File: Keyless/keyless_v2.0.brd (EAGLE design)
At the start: 75 x 48.3 mm, 43 parts, among them J1 AVR_SPI_PRG_6NS, U1 USD-SOCKET, X1 USB-SMD-NS, Y1 16MHz

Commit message: reasons
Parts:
- moved C5 1.09 mm to (58.2, 9.78)
- moved C6 1.02 mm to (60.1, 9.78)
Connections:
- removed net 3.3V1: J1.2
- removed net B10: J1.4
- removed net B8: J1.3
- removed net B9: J1.1
- removed net RESET1: J1.5
- net 3.3V: now also J1.2
- net B1: now also J1.3
- net B2: now also J1.4
- net B3: now also J1.1
- net RESET: now also J1.5
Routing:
- net RAW: track 0.00 -> 44.1 mm
- net 5V: track 0.00 -> 41.2 mm
- net N$1: track 0.00 -> 18.5 mm
- net GND: track 0.00 -> 16.6 mm
- net D6: track 0.00 -> 15.8 mm
- net D7: track 0.00 -> 14.2 mm
- net B4: track 0.00 -> 12.7 mm
- net B1: track 0.00 -> 12.1 mm
- net B3: track 0.00 -> 12.1 mm
- net B2: track 0.00 -> 11.4 mm
- net N$12: track 0.00 -> 9.21 mm
- net N$6: track 0.00 -> 8.98 mm
- net N$5: track 0.00 -> 7.75 mm
- net N$4: track 0.00 -> 6.89 mm
- net UVCC: track 0.00 -> 6.44 mm
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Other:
- board text added: "HackManhattan"
- board text added: "KONSGN"

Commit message: more wires!
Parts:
- moved R9 20.1 mm to (45.8, 9.65)
- moved SJ1 19.7 mm to (42.4, 9.65)
- moved X1 19.7 mm to (47.1, 3.94)
- moved R8 19.6 mm to (47.5, 9.65)
- moved JP2 15.2 mm to (27.3, 3.68)
- moved U$3 13.6 mm to (33.8, 11.7)
- moved C13 13.6 mm to (30.1, 13.0)
- moved C19 13.6 mm to (30.1, 10.5)
- moved U$1 4.45 mm to (39.5, 4.83)
- moved R10 3.83 mm to (37.7, 9.40)
- moved J1 3.07 mm to (40.9, 15.9)
- moved C1 0.81 mm to (49.7, 15.2)
- moved C5 0.51 mm to (58.7, 9.78)
- moved R12 0.51 mm to (67.6, 33.8)
- moved R13 0.51 mm to (65.3, 33.8)
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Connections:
- removed net RAW: C19.1, JP2.2, SJ1.1, U$3.3
- net 5V: now also C19.1, JP2.2, SJ1.1, U$3.3
- net B7: now also JP1.7
- net D5: no longer JP1.7
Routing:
- net 5V: track 41.2 -> 128.4 mm
- net B2: track 11.4 -> 56.8 mm, vias 0 -> 2
- net RAW: track 44.1 -> 0.00 mm
- net B0: track 0.00 -> 42.0 mm, vias 0 -> 1
- net B1: track 12.1 -> 51.3 mm, vias 0 -> 1
- net B3: track 12.1 -> 50.9 mm, vias 0 -> 1
- net 3.3V: track 3.85 -> 37.5 mm, vias 0 -> 1
- net RESET: track 5.32 -> 36.7 mm, vias 0 -> 2
- net UVCC: track 6.44 -> 33.5 mm
- net B7: track 0.00 -> 18.8 mm, vias 0 -> 2
- net D+: track 0.00 -> 14.6 mm
- net D-: track 0.00 -> 14.5 mm
- net GND: track 16.6 -> 21.3 mm
- net N$12: track 9.21 -> 10.3 mm
- net AREF: track 2.03 -> 2.72 mm
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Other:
- outline, holes or cut-outs redrawn
- board text added: "BY:"
- board text added: "Konstantin"
- board text added: "Nickolai"

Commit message: more routing!
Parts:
- moved R13 1.82 mm to (64.9, 35.6)
- moved R12 1.82 mm to (67.2, 35.6)
- moved R7 1.82 mm to (69.5, 35.6)
- moved D3 1.82 mm to (64.9, 38.6)
- moved D1 1.82 mm to (69.5, 38.6)
- moved D2 1.82 mm to (67.2, 38.6)
- moved C2 0.50 mm to (71.9, 20.6)
- moved C4 0.50 mm to (71.9, 15.5)
- moved Y1 0.50 mm to (68.8, 18.0)
- moved C1 0.45 mm to (49.7, 15.7)
- moved R10 0.40 mm to (37.3, 9.27)
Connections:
- removed net N$20: U1.CD1
- removed net N$21: U1.CD2
- net F4: now also U1.CD1
- net GND: now also U1.CD2
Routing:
- net B5: track 0.00 -> 105.6 mm
- net 3.3V: track 37.5 -> 130.9 mm, vias 1 -> 6
- net F4: track 0.00 -> 34.0 mm, vias 0 -> 1
- net F0: track 2.16 -> 31.3 mm
- net D4: track 0.00 -> 28.8 mm, vias 0 -> 2
- net F1: track 3.87 -> 17.7 mm
- net GND: track 21.3 -> 12.8 mm, vias 0 -> 21
- net D0: track 0.00 -> 7.12 mm, vias 0 -> 1
- net B7: track 18.8 -> 20.2 mm
- net N$12: track 10.3 -> 10.9 mm
- net RESET: track 36.7 -> 37.3 mm
- net D6: track 16.1 -> 16.7 mm
- net D7: track 14.6 -> 15.2 mm

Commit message: more stuffs
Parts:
- moved JP3 29.5 mm to (91.6, 27.3), turned to 0 degrees
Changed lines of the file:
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@@
 <setting verticaltext="up"/>
 </settings>
-<grid distance="0.1" unitdist="mm" unit="mm" style="lines" multiple="1" display="yes" altdistance="0.025" altunitdist="inch" altunit="inch"/>
+<grid distance="1.25" unitdist="mil" unit="mil" style="lines" multiple="1" display="yes" altdistance="0.025" altunitdist="inch" altunit="inch"/>
 <layers>
 <layer number="1" name="Top" color="4" fill="1" visible="yes" active="yes"/>
@@
 <element name="R13" library="SparkFun" package="0805" value="330" x="64.878" y="35.56" rot="R90"/>
 <element name="D3" library="led" package="CHIP-LED0805" value="Green" x="64.878" y="38.608"/>
-<element name="JP3" library="SparkFun-Connectors" package="1X08" value="" x="73.406" y="4.064" rot="R180"/>
+<element name="JP3" library="SparkFun-Connectors" package="1X08" value="" x="91.60795" y="27.251390625"/>
 </elements>
 <signals>

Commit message: more
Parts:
- moved JP3 61.4 mm to (30.3, 30.0)
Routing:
- net GND: track 12.8 -> 15.1 mm
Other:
- board text added: "5V in"
- board text added: "GND"
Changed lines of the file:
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@@
 <layer number="27" name="tValues" color="7" fill="1" visible="no" active="yes"/>
 <layer number="28" name="bValues" color="7" fill="1" visible="no" active="yes"/>
-<layer number="29" name="tStop" color="7" fill="3" visible="no" active="yes"/>
-<layer number="30" name="bStop" color="7" fill="6" visible="no" active="yes"/>
+<layer number="29" name="tStop" color="7" fill="3" visible="yes" active="yes"/>
+<layer number="30" name="bStop" color="7" fill="6" visible="yes" active="yes"/>
 <layer number="31" name="tCream" color="7" fill="4" visible="no" active="yes"/>
 <layer number="32" name="bCream" color="7" fill="5" visible="no" active="yes"/>
@@
 <hole x="73.4" y="16" drill="0.6"/>
 <hole x="73.4" y="18.35" drill="0.6"/>
-<rectangle x1="73.5" y1="13" x2="74.5" y2="15" layer="1"/>
+<rectangle x1="73.5" y1="13" x2="74.5" y2="15" layer="16"/>
 <rectangle x1="70.5" y1="18.7" x2="72" y2="19.7" layer="16" rot="R180"/>
-<rectangle x1="73.5" y1="19.35" x2="74.5" y2="21.35" layer="1"/>
+<rectangle x1="73.5" y1="19.35" x2="74.5" y2="21.35" layer="16"/>
+<rectangle x1="70.485" y1="18.669" x2="72.04075" y2="19.71675" layer="22"/>
+<rectangle x1="70.485" y1="14.6685" x2="72.04075" y2="15.71625" layer="22"/>
+<rectangle x1="73.4695" y1="19.33575" x2="74.51725" y2="21.36775" layer="22"/>
+<rectangle x1="73.4695" y1="12.98575" x2="74.51725" y2="15.01775" layer="22"/>
+<text x="37.5285" y="0.3175" size="1.778" layer="21" rot="R90">5V in</text>
+<text x="23.01875" y="1.23825" size="1.778" layer="21" rot="R90">GND</text>
 </plain>
 <attributes>
@@
 <element name="R13" library="SparkFun" package="0805" value="330" x="64.878" y="35.56" rot="R90"/>
 <element name="D3" library="led" package="CHIP-LED0805" value="Green" x="64.878" y="38.608"/>
-<element name="JP3" library="SparkFun-Connectors" package="1X08" value="" x="91.60795" y="27.251390625"/>
+<element name="JP3" library="SparkFun-Connectors" package="1X08" value="" x="30.26695" y="30.045390625"/>
 </elements>
 <signals>
@@
 <via x="62.738" y="17.78" extent="1-16" drill="0.6"/>
 <via x="73.642" y="10.434" extent="1-16" drill="0.6"/>
+<wire x1="71.21525" y1="16.35125" x2="71.3105" y2="16.35125" width="0.4064" layer="16"/>
+<wire x1="71.3105" y1="16.35125" x2="71.3105" y2="14.12875" width="0.4064" layer="16"/>
 </signal>
 <signal name="5V">
@@
 <wire x1="36.41" y1="11.557" x2="36.3855" y2="11.049" width="0.6096" layer="1"/>
 <wire x1="37.211" y1="10.2235" x2="37.338" y2="10.121" width="0.6096" layer="1"/>
-<wire x1="27.07" y1="19.82" x2="27.07" y2="21.101" width="0.4064" layer="16"/>
-<wire x1="27.07" y1="21.101" x2="27.178" y2="21.209" width="0.4064" layer="16"/>
-<via x="27.178" y="21.209" extent="1-16" drill="0.6" diameter="0.254"/>
-<wire x1="27.178" y1="21.209" x2="27.178" y2="18.542" width="0.4064" layer="1"/>
+<wire x1="27.07" y1="19.82" x2="27.07" y2="21.228" width="0.4064" layer="16"/>
+<wire x1="27.07" y1="21.228" x2="27.178" y2="21.336" width="0.4064" layer="16"/>
+<via x="27.178" y="21.336" extent="1-16" drill="0.6" diameter="0.254"/>
+<wire x1="27.178" y1="21.336" x2="27.178" y2="18.542" width="0.4064" layer="1"/>
 <wire x1="27.178" y1="18.542" x2="30.988" y2="14.732" width="0.4064" layer="1"/>
 <wire x1="30.988" y1="14.732" x2="30.988" y2="12.993" width="0.4064" layer="1"/>

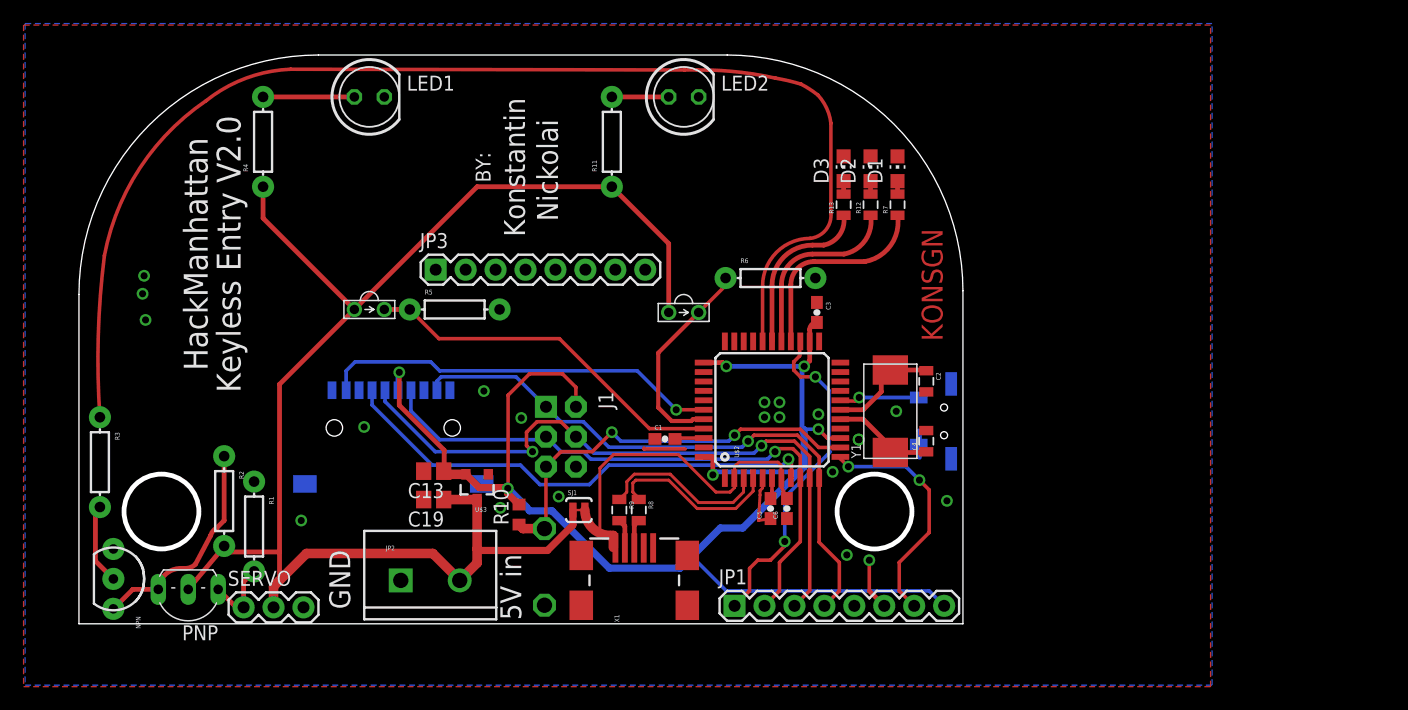
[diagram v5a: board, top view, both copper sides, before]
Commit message: added pin breakouts
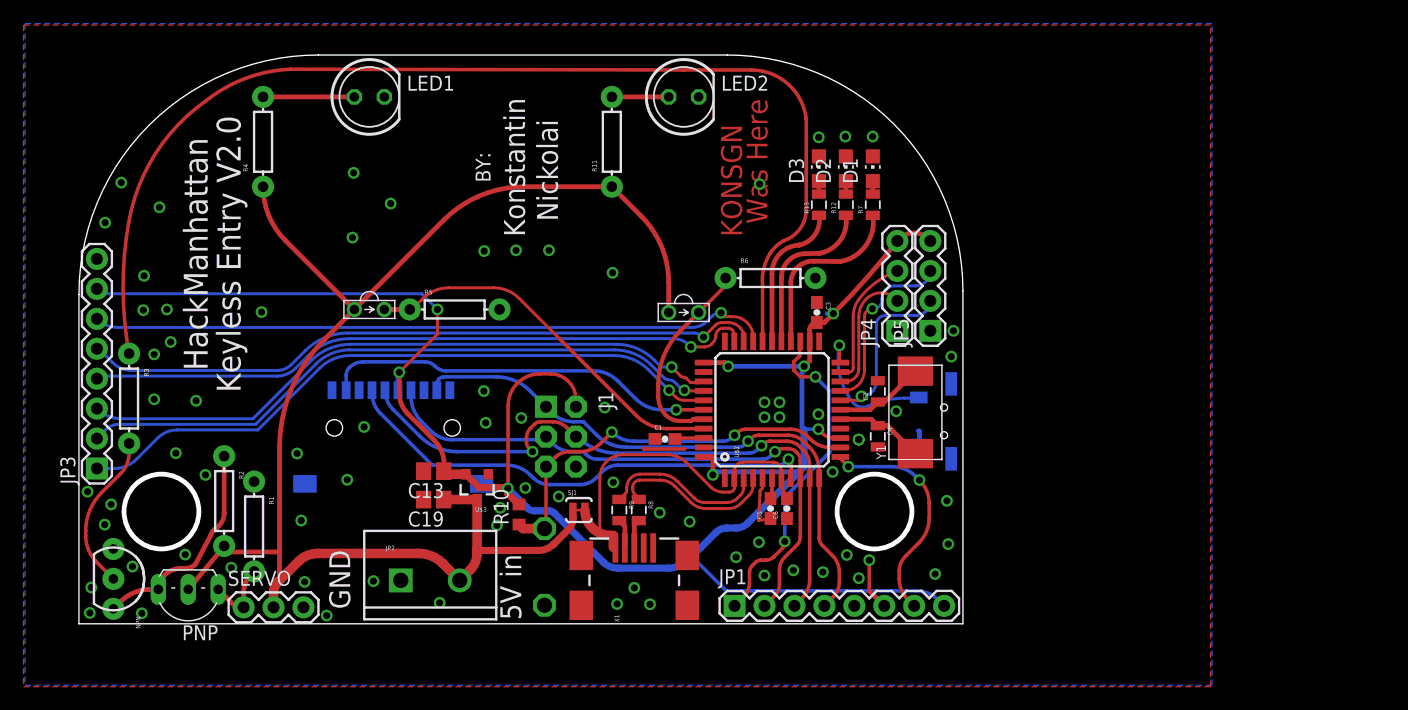
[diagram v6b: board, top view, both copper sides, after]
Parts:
- added JP4, JP5: (no value), SparkFun-Connectors:1X04
- moved JP3 33.3 mm to (1.52, 13.2), turned to 90 degrees
- moved R3 5.94 mm to (4.25, 19.1)
- moved C2 4.20 mm to (67.8, 19.7), turned to 90 degrees
- moved C4 4.13 mm to (67.8, 15.9), turned to 270 degrees
- moved Y1 2.13 mm to (71.0, 17.9)
- moved D1 2.10 mm to (67.4, 38.6)
- moved D2 2.10 mm to (65.1, 38.6)
- moved D3 2.10 mm to (62.8, 38.6)
- moved R12 2.10 mm to (65.1, 35.6)
- moved R13 2.10 mm to (62.8, 35.6)
- moved R7 2.10 mm to (67.4, 35.6)
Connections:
- net 3.3V: now also JP3.7, JP4.4, JP5.4
- net B6: now also JP3.6
- net C6: now also JP3.5
- net C7: now also JP3.4
- net D0: now also JP5.2
- net D1: now also JP5.3
- net D2: now also JP4.2
- net D3: now also JP4.3
- net F5: now also JP3.1
- net F6: now also JP3.2
- net F7: now also JP3.3
- net GND: now also JP3.8, JP4.1, JP5.1
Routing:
- net C6: track 0.00 -> 58.0 mm, vias 0 -> 1
- net B6: track 0.00 -> 57.4 mm, vias 0 -> 1
- net C7: track 0.00 -> 56.9 mm, vias 0 -> 1
- net F5: track 0.00 -> 56.2 mm, vias 0 -> 1
- net F7: track 0.00 -> 55.8 mm, vias 0 -> 1
- net F6: track 0.00 -> 55.3 mm, vias 0 -> 1
- net 3.3V: track 131.2 -> 178.4 mm, vias 6 -> 8
- net D1: track 0.00 -> 14.6 mm, vias 0 -> 1
- net D5: track 0.00 -> 13.6 mm, vias 0 -> 1
- net D3: track 0.00 -> 11.2 mm
- net D2: track 0.00 -> 10.7 mm
- net B5: track 105.6 -> 96.4 mm
- net D0: track 7.12 -> 14.0 mm
- net N$4: track 6.89 -> 13.3 mm
- net N$12: track 10.9 -> 7.73 mm
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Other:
- board text added: "Was Here"

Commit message: Finalized!
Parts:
- moved C19 0.16 mm to (30.1, 10.7)
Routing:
- net 3.3V: track 178.4 -> 183.0 mm
- net F7: track 55.8 -> 55.2 mm
- net F6: track 55.3 -> 54.7 mm
- net F5: track 56.2 -> 55.6 mm
- net GND: vias 77 -> 81
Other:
- board text added: "0-CE"
- board text added: "10"
- board text added: "11"
- board text added: "12"
- board text added: "13"
- board text added: "15-A6"
- board text added: "16-A5"
- board text added: "17-A4"
- board text added: "18-A3"
- board text added: "19- CD"
- board text added: "22"
- board text added: "3.3V"
- board text added: "3V3"
- board text added: "4"
- board text added: "9"
- board text added: "A0-21"
- board text added: "A1-20"
- board text added: "B1"
- board text added: "B2"
- board text added: "B3"
- board text added: "B6"
- board text added: "B7"
- board text added: "C6"
- board text added: "C7"
- board text added: "D4"
- board text added: "DON'T PRESS!"
- board text added: "DON'T REMOVE SD!"
- board text added: "Detect Closed"
- board text added: "Detect Lock"
- board text added: "Expansion"
- board text added: "F5"
- board text added: "F6"
- board text added: "F7"
- board text added: "Files Erase!"
- board text added: "MISO"
- board text added: "MOSI"
- board text added: "Many Programming"
- board text added: "Much"
- board text added: "RX"
- board text added: "SCK"
- board text added: "SCL"
- board text added: "SDA"
- board text added: "So USB"
- board text added: "Such Corruption!"
- board text added: "TX"
- board text added: "many GND"
- board text added: "such Reset"
- board text added: "such VIN"

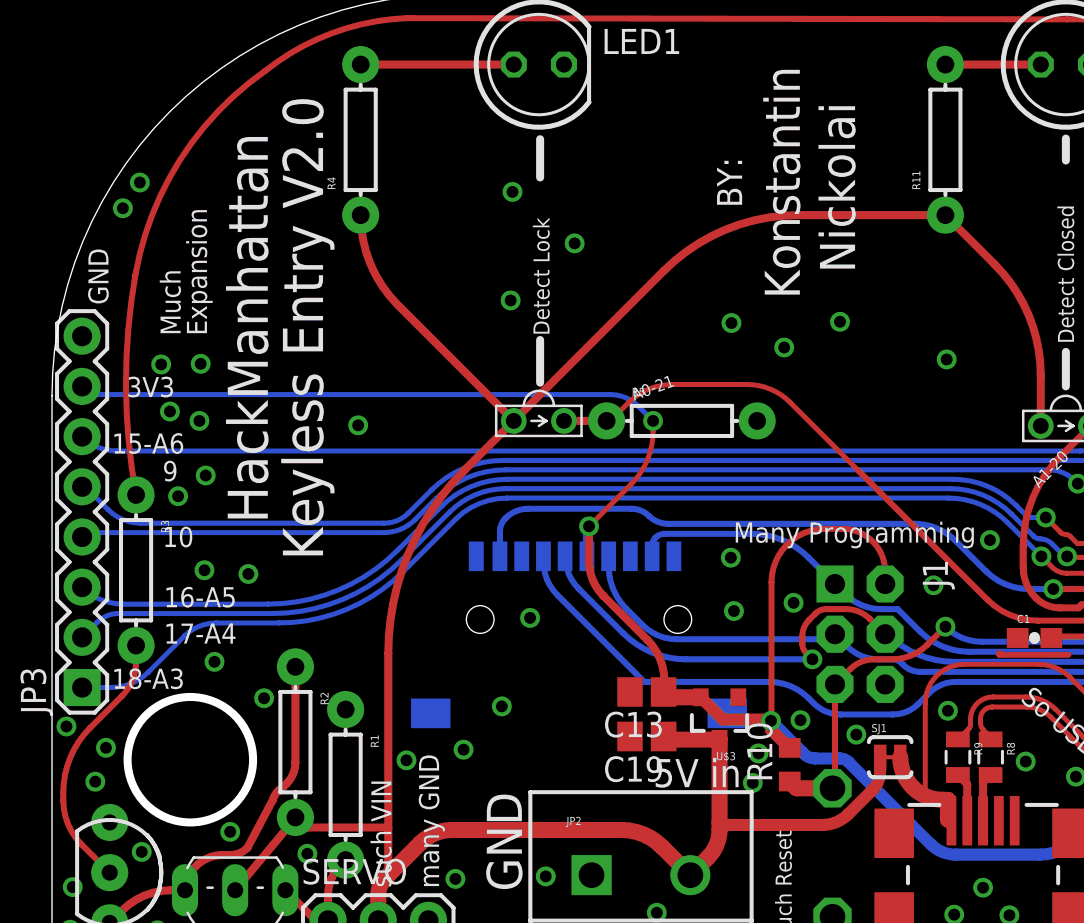
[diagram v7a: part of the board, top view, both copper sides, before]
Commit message: added values & BOM
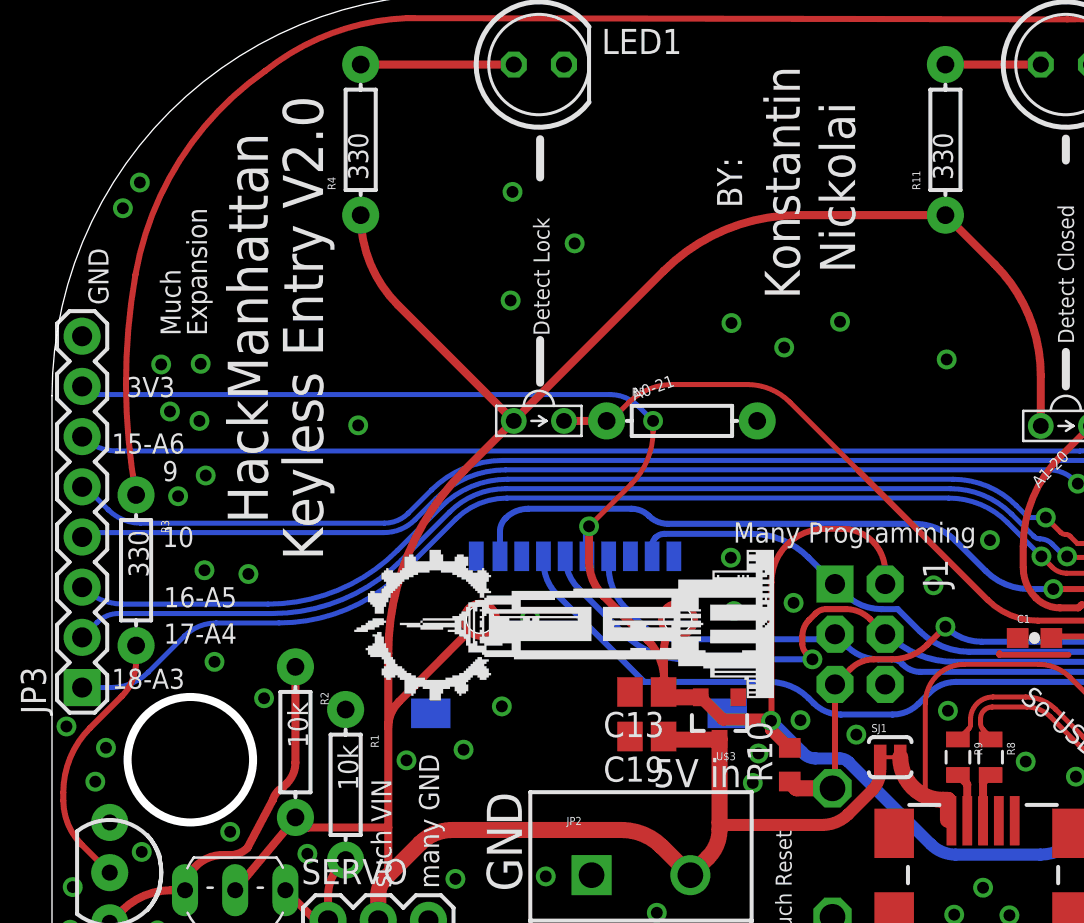
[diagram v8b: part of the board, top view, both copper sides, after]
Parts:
- R1, R10, R2: value (none) -> 10k
- R11, R3, R4: value (none) -> 330
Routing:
- net N$10: track 0.00 -> 7.21 mm
- net N$11: track 0.00 -> 3.10 mm
